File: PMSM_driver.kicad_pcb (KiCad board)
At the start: 2 copper layers, 82 x 79 mm, 80 parts, among them J1 22-23-2021, J2 Screw_Terminal_Power, J3 Screw_Terminal_1, J4 Screw_Terminal_2, J5 Screw_Terminal_3, J6 Screw_Terminal_Logic, J7 302-S101, Q1 IRFH8334, Q2 IRFH8334, Q3 IRFH8334, Q4 IRFH8334, Q5 IRFH8334, Q6 IRFH8334, U1 IR2110, U2 IR2110, U3 IR2110, U4 LM358DT

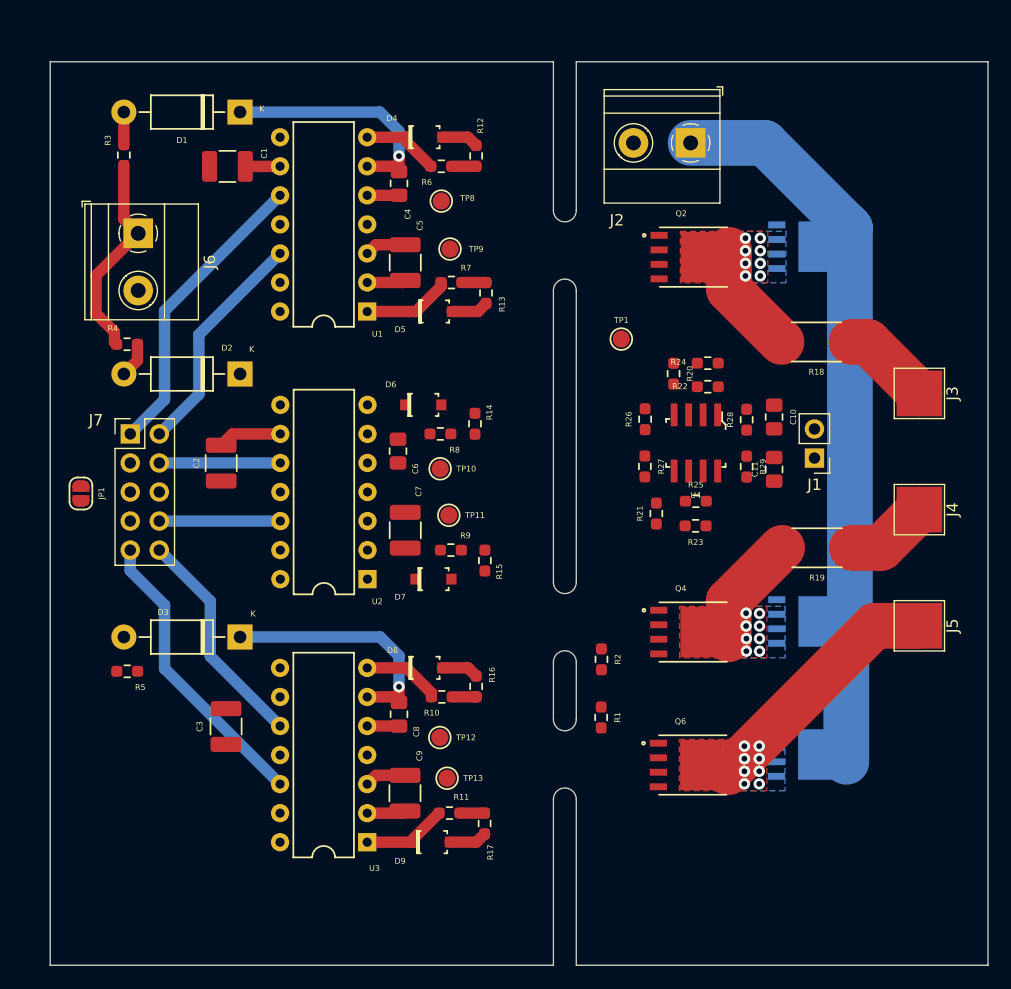
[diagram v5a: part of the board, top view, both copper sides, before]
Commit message: [PCB]: One side placement
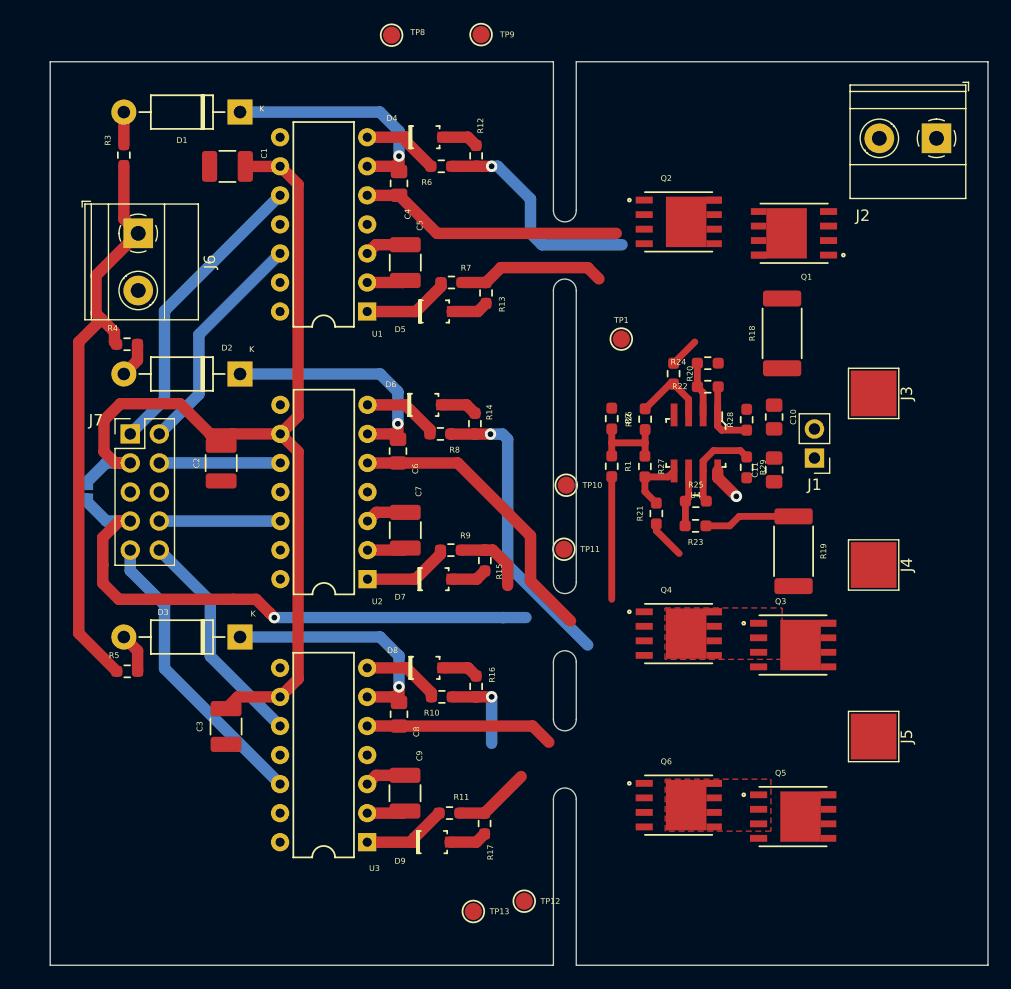
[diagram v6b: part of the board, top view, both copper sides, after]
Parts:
- JP1: moved to B.Cu
- Q1, Q3, Q5: moved to F.Cu
- moved R1 22.0 mm to (147.1, 86.4)
- moved J2 21.5 mm to (175.5, 57.7)
- moved R2 21.1 mm to (147.1, 82.2)
- moved TP9 18.9 mm to (135.7, 48.6)
- moved TP12 16.1 mm to (139.4, 124.4)
- moved TP8 15.1 mm to (127.8, 48.7)
- moved TP13 11.9 mm to (135.0, 125.3)
- moved TP10 11.1 mm to (143.1, 88.0)
- moved TP11 10.5 mm to (142.9, 93.6)
- moved J5 10.5 mm to (170.0, 110.0)
- moved J4 6.28 mm to (170.0, 95.0)
- moved Q5 5.64 mm to (163.0, 117.0)
- moved J3 4.00 mm to (170.0, 80.0)
- moved Q6 3.72 mm to (153.0, 116.0)
- moved Q2 3.34 mm to (153.0, 65.0)
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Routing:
- net VDD: track 8.63 -> 87.4 mm
- net +VDC: track 63.8 -> 2.90 mm, vias 0 -> 1
- net +3.3V: track 0.00 -> 60.7 mm, vias 0 -> 1
- net VCC: track 25.7 -> 62.3 mm
- net Net-(Q3-Pad4): track 0.00 -> 26.1 mm, vias 0 -> 1
- net Net-(C6-Pad1): track 0.00 -> 21.5 mm, vias 0 -> 1
- net /Q3_Q4: track 9.94 -> 29.2 mm, vias 8 -> 0
- net Net-(Q1-Pad4): track 2.14 -> 19.5 mm, vias 0 -> 1
- net /Q1_Q2: track 12.7 -> 25.8 mm, vias 8 -> 0
- net Net-(Q2-Pad4): track 2.11 -> 12.9 mm
- net PHASE_3: track 24.8 -> 16.5 mm, vias 8 -> 0
- net Net-(R25-Pad2): track 0.00 -> 8.04 mm
- net PHASE_1: track 7.81 -> 0.00 mm
- net Net-(D7-PadK): track 0.00 -> 7.64 mm
- net 1V65: track 0.00 -> 7.59 mm
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- removed copper zone on B.Cu, net /Q1_Q2
- removed copper zone on F.Cu, net /Q1_Q2
- removed copper zone on B.Cu, net /Q3_Q4
- removed copper zone on B.Cu, net PHASE_3

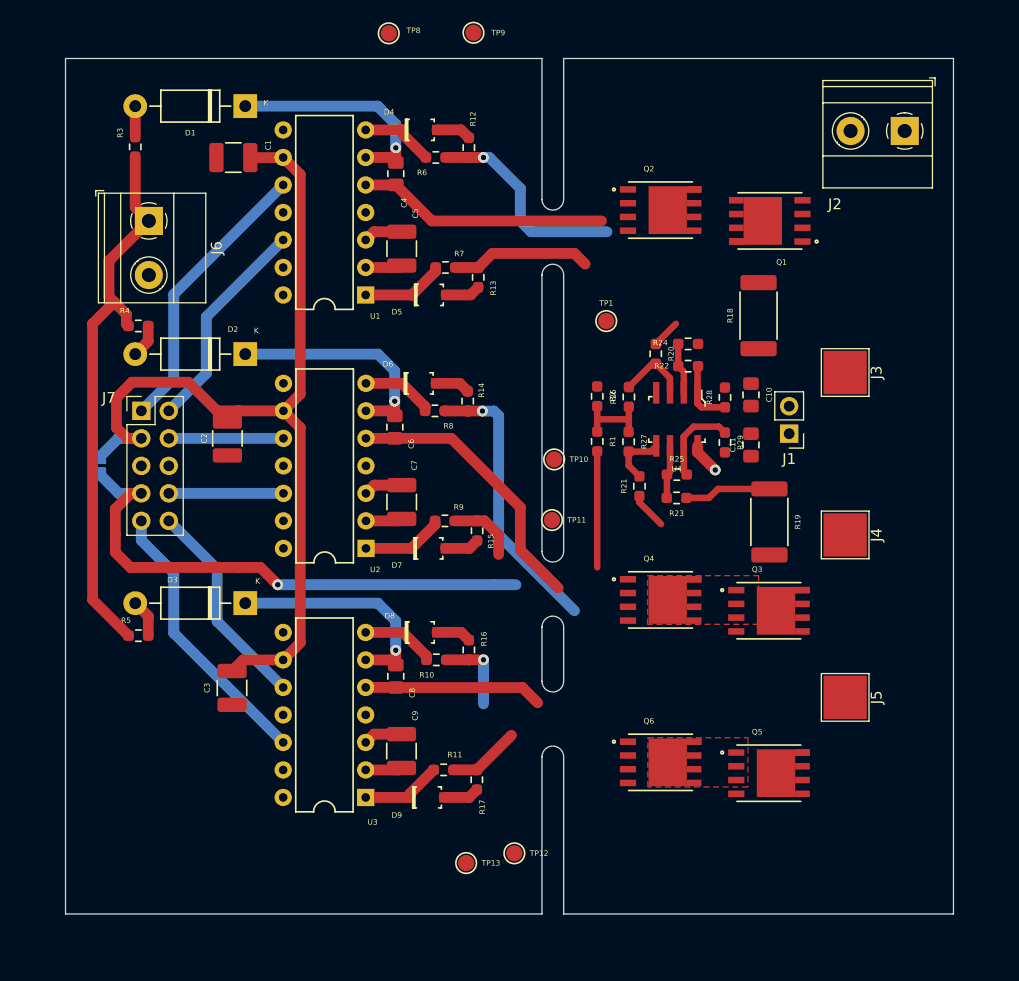
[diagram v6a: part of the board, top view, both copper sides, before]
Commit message: [PCB]: added output connectors for another MOSFETs board
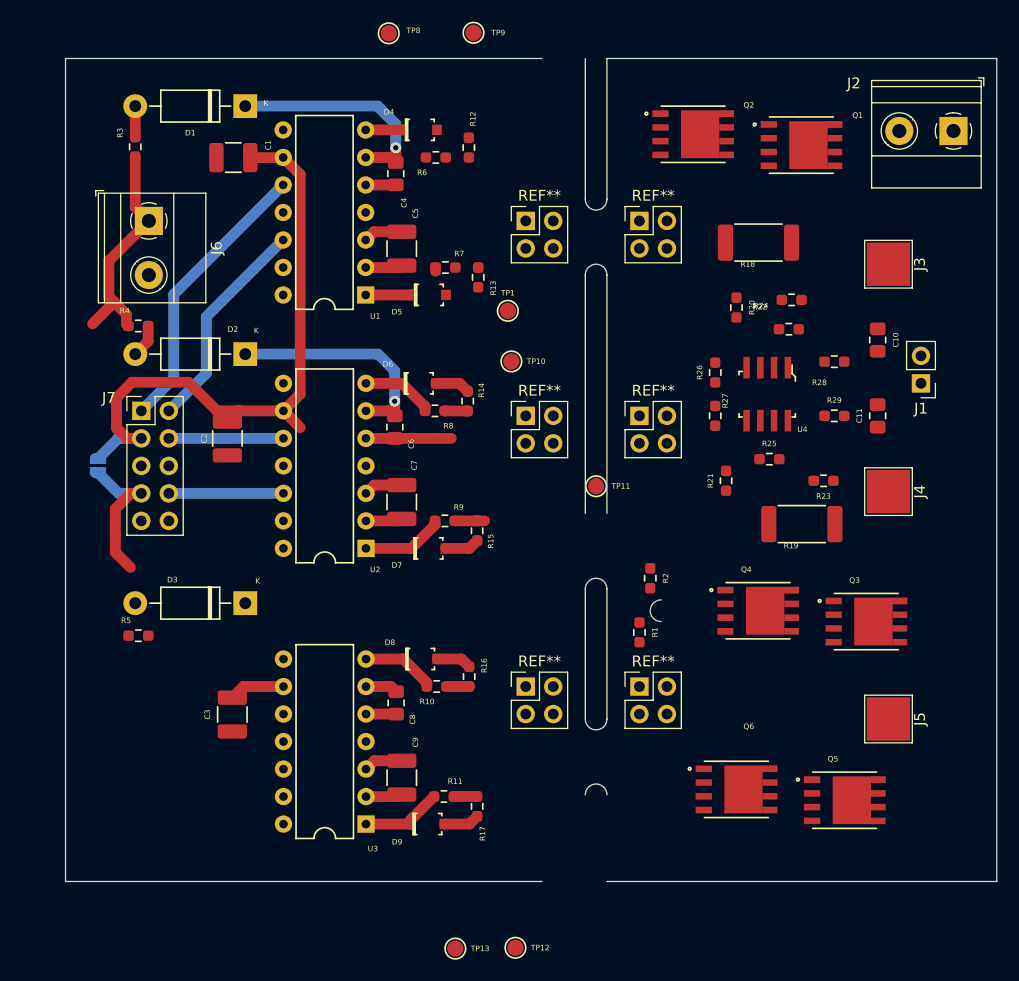
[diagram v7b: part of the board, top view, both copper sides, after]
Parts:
- added REF**: PinHeader_1, Connector_PinHeader_2.54mm:PinHeader_2x02_P2.54mm_Vertical, F.Cu at (140.5, 66.0)
- added REF**: PinHeader_1, Connector_PinHeader_2.54mm:PinHeader_2x02_P2.54mm_Vertical, F.Cu at (151.0, 66.0)
- added REF**: PinHeader_1, Connector_PinHeader_2.54mm:PinHeader_2x02_P2.54mm_Vertical, F.Cu at (151.0, 84.0)
- added REF**: PinHeader_1, Connector_PinHeader_2.54mm:PinHeader_2x02_P2.54mm_Vertical, F.Cu at (140.5, 84.0)
- added REF**: PinHeader_1, Connector_PinHeader_2.54mm:PinHeader_2x02_P2.54mm_Vertical, F.Cu at (151.0, 109.0)
- added REF**: PinHeader_1, Connector_PinHeader_2.54mm:PinHeader_2x02_P2.54mm_Vertical, F.Cu at (140.5, 109.0)
- moved R1 18.1 mm to (151.0, 104.0)
- moved R2 17.5 mm to (152.0, 99.0)
- moved R23 13.7 mm to (168.0, 90.0)
- moved J1 13.0 mm to (177.0, 81.0)
- moved C10 12.7 mm to (173.0, 77.0)
- moved C11 12.0 mm to (173.0, 84.0)
- moved J3 10.8 mm to (174.0, 70.0)
- moved R28 10.6 mm to (169.0, 79.0), turned to 180 degrees
- moved R29 10.4 mm to (169.0, 84.0), turned to 0 degrees
- moved R22 10.4 mm to (165.1, 73.3)
- moved R24 9.91 mm to (164.8, 76.0)
- moved TP10 9.87 mm to (139.2, 79.0)
- moved TP1 9.14 mm to (138.8, 74.3)
- moved Q3 9.06 mm to (172.0, 103.0)
- moved Q4 9.06 mm to (162.0, 102.0)
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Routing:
- net +3.3V: track 60.7 -> 13.8 mm, vias 1 -> 0
- net VCC: track 62.3 -> 32.1 mm
- net /L3: track 25.9 -> 0.00 mm
- net Net-(Q3-Pad4): track 26.1 -> 2.15 mm, vias 1 -> 0
- net /Q1_Q2: track 25.8 -> 2.78 mm
- net VDD: track 87.4 -> 65.3 mm
- net /Q3_Q4: track 29.2 -> 7.88 mm
- net /H3: track 19.8 -> 0.00 mm
- net Net-(Q1-Pad4): track 19.5 -> 0.00 mm, vias 1 -> 0
- net Net-(C8-Pad1): track 21.6 -> 2.98 mm, vias 1 -> 0
- net PHASE_3: track 16.5 -> 2.78 mm
- net Net-(Q2-Pad4): track 12.9 -> 0.00 mm
- net Net-(R25-Pad2): track 8.04 -> 0.00 mm
- net PHASE_2: track 8.00 -> 0.00 mm
- net 1V65: track 7.59 -> 0.00 mm
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- removed copper zone on F.Cu, net /Q3_Q4
- removed copper zone on F.Cu, net PHASE_3
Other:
- board size 82 x 79 mm -> 86 x 76 mm

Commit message: [PCB]: Power board layout completion
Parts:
- moved R1 12.6 mm to (155.0, 92.0), turned to 180 degrees
- moved R23 5.31 mm to (163.0, 88.2)
- moved R2 5.00 mm to (156.0, 96.0), turned to 90 degrees
- moved C11 4.47 mm to (169.0, 86.0)
- moved J1 4.24 mm to (174.0, 84.0)
- moved R20 4.08 mm to (156.0, 73.0)
- moved R21 3.93 mm to (158.0, 86.2)
- moved R24 3.77 mm to (168.0, 74.0)
- moved U4 3.01 mm to (163.0, 79.0)
- moved R26 3.00 mm to (158.0, 77.0)
- moved R29 3.00 mm to (169.0, 81.0), turned to -90 degrees
- moved R25 2.80 mm to (163.0, 85.2)
- moved R27 2.80 mm to (158.0, 81.2)
- moved R19 2.24 mm to (164.0, 93.0)
- moved R22 2.08 mm to (163.0, 73.0), turned to 0 degrees
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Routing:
- net +VDC: track 0.00 -> 91.2 mm
- net 1V65: track 0.00 -> 21.0 mm
- net PHASE_3: track 2.78 -> 23.5 mm
- net /Q3_Q4: track 7.88 -> 28.3 mm
- net /Q1_Q2: track 2.78 -> 22.0 mm
- net PHASE_1: track 0.00 -> 17.0 mm
- net PHASE_2: track 0.00 -> 14.9 mm
- net Net-(R25-Pad2): track 0.00 -> 11.7 mm
- net Net-(R20-Pad2): track 0.00 -> 10.0 mm
- net /CUR_OUT_2: track 0.00 -> 8.45 mm
- net /CUR_OUT_1: track 0.00 -> 7.94 mm
- net Net-(R24-Pad2): track 0.00 -> 6.92 mm
- net Net-(R23-Pad2): track 0.00 -> 6.86 mm
- net Net-(R22-Pad2): track 0.00 -> 6.70 mm
- net Net-(R21-Pad2): track 0.00 -> 6.54 mm
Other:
- outline, holes or cut-outs redrawn
